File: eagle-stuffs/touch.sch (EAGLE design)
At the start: 6 parts, among them U1 AT42QT1010SOT23

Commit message: Updated something
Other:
- moved on the sheet: C7, C8, R1, SENSE, TOUCH, U1
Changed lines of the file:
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@@
 </plain>
 <instances>
-<instance part="U1" gate="G$1" x="132.08" y="109.22"/>
-<instance part="R1" gate="G$1" x="177.8" y="114.3" rot="R180"/>
-<instance part="C7" gate="G$1" x="167.64" y="109.22"/>
-<instance part="SUPPLY10" gate="+5V" x="132.08" y="134.62"/>
-<instance part="SUPPLY13" gate="GND" x="114.3" y="86.36"/>
-<instance part="C8" gate="G$1" x="104.14" y="109.22"/>
+<instance part="U1" gate="G$1" x="121.92" y="111.76"/>
+<instance part="R1" gate="G$1" x="167.64" y="116.84" rot="R180"/>
+<instance part="C7" gate="G$1" x="154.94" y="111.76" rot="R270"/>
+<instance part="SUPPLY10" gate="+5V" x="121.92" y="137.16"/>
+<instance part="SUPPLY13" gate="GND" x="104.14" y="88.9"/>
+<instance part="C8" gate="G$1" x="93.98" y="111.76"/>
 <instance part="FRAME1" gate="G$1" x="0" y="0"/>
 <instance part="FRAME1" gate="G$2" x="172.72" y="2.54"/>
-<instance part="TOUCH" gate="A" x="200.66" y="111.76"/>
-<instance part="SENSE" gate="G$1" x="200.66" y="99.06"/>
+<instance part="TOUCH" gate="A" x="190.5" y="114.3"/>
+<instance part="SENSE" gate="G$1" x="190.5" y="101.6"/>
 </instances>
 <busses>
@@
 <segment>
 <pinref part="U1" gate="G$1" pin="VSS"/>
-<wire x1="114.3" y1="104.14" x2="114.3" y2="93.98" width="0.1524" layer="91"/>
+<wire x1="104.14" y1="106.68" x2="104.14" y2="96.52" width="0.1524" layer="91"/>
 <pinref part="SUPPLY13" gate="GND" pin="GND"/>
 <pinref part="C8" gate="G$1" pin="2"/>
-<wire x1="114.3" y1="93.98" x2="114.3" y2="88.9" width="0.1524" layer="91"/>
-<wire x1="114.3" y1="93.98" x2="104.14" y2="93.98" width="0.1524" layer="91"/>
-<wire x1="104.14" y1="93.98" x2="104.14" y2="104.14" width="0.1524" layer="91"/>
-<junction x="114.3" y="93.98"/>
-<wire x1="114.3" y1="93.98" x2="205.74" y2="93.98" width="0.1524" layer="91"/>
-<wire x1="205.74" y1="93.98" x2="205.74" y2="109.22" width="0.1524" layer="91"/>
-<junction x="114.3" y="93.98"/>
+<wire x1="104.14" y1="96.52" x2="104.14" y2="91.44" width="0.1524" layer="91"/>
+<wire x1="104.14" y1="96.52" x2="93.98" y2="96.52" width="0.1524" layer="91"/>
+<wire x1="93.98" y1="96.52" x2="93.98" y2="106.68" width="0.1524" layer="91"/>
+<junction x="104.14" y="96.52"/>
+<wire x1="104.14" y1="96.52" x2="195.58" y2="96.52" width="0.1524" layer="91"/>
+<wire x1="195.58" y1="96.52" x2="195.58" y2="111.76" width="0.1524" layer="91"/>
+<junction x="104.14" y="96.52"/>
 <pinref part="TOUCH" gate="A" pin="3"/>
-<wire x1="205.74" y1="109.22" x2="198.12" y2="109.22" width="0.1524" layer="91"/>
+<wire x1="195.58" y1="111.76" x2="187.96" y2="111.76" width="0.1524" layer="91"/>
 </segment>
 </net>
@@
 <pinref part="U1" gate="G$1" pin="VDD"/>
 <pinref part="U1" gate="G$1" pin="SYNC/MODE"/>
-<wire x1="132.08" y1="132.08" x2="132.08" y2="124.46" width="0.1524" layer="91"/>
-<wire x1="149.86" y1="104.14" x2="154.94" y2="104.14" width="0.1524" layer="91"/>
-<wire x1="154.94" y1="104.14" x2="154.94" y2="132.08" width="0.1524" layer="91"/>
-<wire x1="154.94" y1="132.08" x2="132.08" y2="132.08" width="0.1524" layer="91"/>
-<junction x="132.08" y="132.08"/>
+<wire x1="121.92" y1="134.62" x2="121.92" y2="127" width="0.1524" layer="91"/>
+<wire x1="139.7" y1="106.68" x2="144.78" y2="106.68" width="0.1524" layer="91"/>
+<wire x1="144.78" y1="106.68" x2="144.78" y2="134.62" width="0.1524" layer="91"/>
+<wire x1="144.78" y1="134.62" x2="121.92" y2="134.62" width="0.1524" layer="91"/>
+<junction x="121.92" y="134.62"/>
 <pinref part="C8" gate="G$1" pin="1"/>
-<wire x1="132.08" y1="132.08" x2="104.14" y2="132.08" width="0.1524" layer="91"/>
-<wire x1="104.14" y1="132.08" x2="104.14" y2="111.76" width="0.1524" layer="91"/>
-<wire x1="154.94" y1="132.08" x2="205.74" y2="132.08" width="0.1524" layer="91"/>
-<wire x1="205.74" y1="132.08" x2="205.74" y2="111.76" width="0.1524" layer="91"/>
-<junction x="154.94" y="132.08"/>
+<wire x1="121.92" y1="134.62" x2="93.98" y2="134.62" width="0.1524" layer="91"/>
+<wire x1="93.98" y1="134.62" x2="93.98" y2="114.3" width="0.1524" layer="91"/>
+<wire x1="144.78" y1="134.62" x2="195.58" y2="134.62" width="0.1524" layer="91"/>
+<wire x1="195.58" y1="134.62" x2="195.58" y2="114.3" width="0.1524" layer="91"/>
+<junction x="144.78" y="134.62"/>
 <pinref part="TOUCH" gate="A" pin="2"/>
-<wire x1="205.74" y1="111.76" x2="198.12" y2="111.76" width="0.1524" layer="91"/>
+<wire x1="195.58" y1="114.3" x2="187.96" y2="114.3" width="0.1524" layer="91"/>
 </segment>
 </net>
@@
 <pinref part="R1" gate="G$1" pin="2"/>
 <pinref part="U1" gate="G$1" pin="SNSK"/>
-<wire x1="172.72" y1="114.3" x2="167.64" y2="114.3" width="0.1524" layer="91"/>
+<wire x1="162.56" y1="116.84" x2="157.48" y2="116.84" width="0.1524" layer="91"/>
 <pinref part="C7" gate="G$1" pin="1"/>
-<wire x1="167.64" y1="114.3" x2="149.86" y2="114.3" width="0.1524" layer="91"/>
-<wire x1="167.64" y1="111.76" x2="167.64" y2="114.3" width="0.1524" layer="91"/>
-<junction x="167.64" y="114.3"/>
+<wire x1="157.48" y1="116.84" x2="139.7" y2="116.84" width="0.1524" layer="91"/>
+<wire x1="157.48" y1="111.76" x2="157.48" y2="116.84" width="0.1524" layer="91"/>
+<junction x="157.48" y="116.84"/>
 </segment>
 </net>
@@
 <segment>
 <pinref part="C7" gate="G$1" pin="2"/>
-<wire x1="167.64" y1="104.14" x2="167.64" y2="101.6" width="0.1524" layer="91"/>
-<wire x1="167.64" y1="101.6" x2="160.02" y2="101.6" width="0.1524" layer="91"/>
-<wire x1="160.02" y1="101.6" x2="160.02" y2="109.22" width="0.1524" layer="91"/>
 <pinref part="U1" gate="G$1" pin="SNS"/>
-<wire x1="160.02" y1="109.22" x2="149.86" y2="109.22" width="0.1524" layer="91"/>
+<wire x1="149.86" y1="111.76" x2="139.7" y2="111.76" width="0.1524" layer="91"/>
 </segment>
 </net>
@@
 <segment>
 <pinref part="U1" gate="G$1" pin="OUT"/>
-<wire x1="114.3" y1="114.3" x2="114.3" y2="127" width="0.1524" layer="91"/>
-<wire x1="114.3" y1="127" x2="190.5" y2="127" width="0.1524" layer="91"/>
-<wire x1="190.5" y1="127" x2="190.5" y2="114.3" width="0.1524" layer="91"/>
+<wire x1="104.14" y1="116.84" x2="104.14" y2="129.54" width="0.1524" layer="91"/>
+<wire x1="104.14" y1="129.54" x2="180.34" y2="129.54" width="0.1524" layer="91"/>
+<wire x1="180.34" y1="129.54" x2="180.34" y2="116.84" width="0.1524" layer="91"/>
 <pinref part="TOUCH" gate="A" pin="1"/>
-<wire x1="190.5" y1="114.3" x2="198.12" y2="114.3" width="0.1524" layer="91"/>
+<wire x1="180.34" y1="116.84" x2="187.96" y2="116.84" width="0.1524" layer="91"/>
 </segment>
 </net>
@@
 <pinref part="SENSE" gate="G$1" pin="1"/>
 <pinref part="R1" gate="G$1" pin="1"/>
-<wire x1="198.12" y1="99.06" x2="182.88" y2="99.06" width="0.1524" layer="91"/>
-<wire x1="182.88" y1="99.06" x2="182.88" y2="114.3" width="0.1524" layer="91"/>
+<wire x1="187.96" y1="101.6" x2="172.72" y2="101.6" width="0.1524" layer="91"/>
+<wire x1="172.72" y1="101.6" x2="172.72" y2="116.84" width="0.1524" layer="91"/>
 </segment>
 </net>

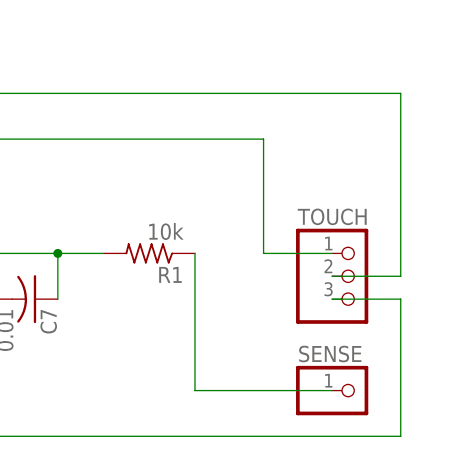
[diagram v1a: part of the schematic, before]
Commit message: Changed some drilling size
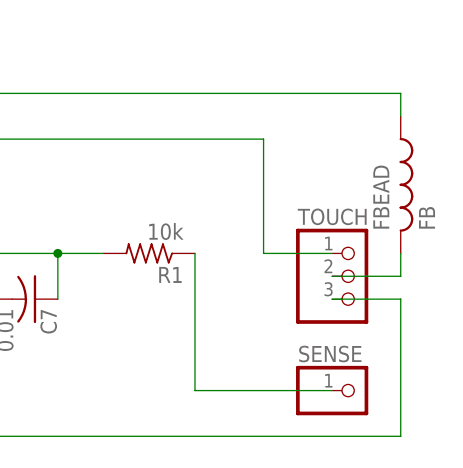
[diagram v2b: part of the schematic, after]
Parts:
- added FBEAD: FB, adafruit:FB
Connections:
- new net N$3: FBEAD.2, TOUCH.2
- net +5V: now also FBEAD.1; no longer TOUCH.2
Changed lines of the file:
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@@
 <part name="TOUCH" library="adafruit" deviceset="PINHD-1X3" device=""/>
 <part name="SENSE" library="adafruit" deviceset="PINHD-1X1" device=""/>
+<part name="FBEAD" library="adafruit" deviceset="FB" device=""/>
 </parts>
 <sheets>
@@
 <instance part="TOUCH" gate="A" x="190.5" y="114.3"/>
 <instance part="SENSE" gate="G$1" x="190.5" y="101.6"/>
+<instance part="FBEAD" gate="G$1" x="195.58" y="124.46"/>
 </instances>
 <busses>
@@
 <wire x1="93.98" y1="134.62" x2="93.98" y2="114.3" width="0.1524" layer="91"/>
 <wire x1="144.78" y1="134.62" x2="195.58" y2="134.62" width="0.1524" layer="91"/>
-<wire x1="195.58" y1="134.62" x2="195.58" y2="114.3" width="0.1524" layer="91"/>
 <junction x="144.78" y="134.62"/>
-<pinref part="TOUCH" gate="A" pin="2"/>
-<wire x1="195.58" y1="114.3" x2="187.96" y2="114.3" width="0.1524" layer="91"/>
+<pinref part="FBEAD" gate="G$1" pin="1"/>
+<wire x1="195.58" y1="134.62" x2="195.58" y2="132.08" width="0.1524" layer="91"/>
 </segment>
 </net>
@@
 </segment>
 </net>
+<net name="N$3" class="0">
+<segment>
+<pinref part="TOUCH" gate="A" pin="2"/>
+<wire x1="195.58" y1="114.3" x2="187.96" y2="114.3" width="0.1524" layer="91"/>
+<pinref part="FBEAD" gate="G$1" pin="2"/>
+<wire x1="195.58" y1="114.3" x2="195.58" y2="116.84" width="0.1524" layer="91"/>
+</segment>
+</net>

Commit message: Added some info
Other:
- moved on the sheet: TOUCH
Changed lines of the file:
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@@
 <instance part="FRAME1" gate="G$1" x="0" y="0"/>
 <instance part="FRAME1" gate="G$2" x="172.72" y="2.54"/>
-<instance part="TOUCH" gate="A" x="190.5" y="114.3"/>
+<instance part="TOUCH" gate="A" x="187.96" y="114.3"/>
 <instance part="SENSE" gate="G$1" x="190.5" y="101.6"/>
 <instance part="FBEAD" gate="G$1" x="195.58" y="124.46"/>
@@
 <junction x="104.14" y="96.52"/>
 <pinref part="TOUCH" gate="A" pin="3"/>
-<wire x1="195.58" y1="111.76" x2="187.96" y2="111.76" width="0.1524" layer="91"/>
+<wire x1="195.58" y1="111.76" x2="185.42" y2="111.76" width="0.1524" layer="91"/>
 </segment>
 </net>
@@
 <wire x1="180.34" y1="129.54" x2="180.34" y2="116.84" width="0.1524" layer="91"/>
 <pinref part="TOUCH" gate="A" pin="1"/>
-<wire x1="180.34" y1="116.84" x2="187.96" y2="116.84" width="0.1524" layer="91"/>
+<wire x1="180.34" y1="116.84" x2="185.42" y2="116.84" width="0.1524" layer="91"/>
 </segment>
 </net>
@@
 <segment>
 <pinref part="TOUCH" gate="A" pin="2"/>
-<wire x1="195.58" y1="114.3" x2="187.96" y2="114.3" width="0.1524" layer="91"/>
+<wire x1="195.58" y1="114.3" x2="185.42" y2="114.3" width="0.1524" layer="91"/>
 <pinref part="FBEAD" gate="G$1" pin="2"/>
 <wire x1="195.58" y1="114.3" x2="195.58" y2="116.84" width="0.1524" layer="91"/>
